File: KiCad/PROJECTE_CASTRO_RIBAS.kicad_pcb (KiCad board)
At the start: 2 copper layers, 114.1 x 85.8 mm, 72 parts, among them J1 DE9_Pins, J2 DE9_Pins, J3 Conn_01x05, J4 Conn_01x02_Pin, J5 Conn_01x04_Pin, K1 Fujitsu_FTR-LYAA005x, K2 Fujitsu_FTR-LYAA005x, SW3 SW_Push_Dual, SW4 SW_Push, SW5 SW_Push, U1 LM2596S-12, U2 LM1117DT-3.3, U20 PIC24HJ128GP502, U23 FXTH87, U3 SN65HVD230, U4 MAX3232, U6 FDC2214, Y1 Crystal

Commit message: Pin del micro pel modul RF triat
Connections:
- U20 pad 11: unconnected-(U20-RB4-Pad11) -> RF_data
- U20 pad 21: CNTRL -> unconnected-(U20-RB10-Pad21)
- U20 pad 22: PWM -> unconnected-(U20-RB11-Pad22)
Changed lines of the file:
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@@
 	(net 75 "unconnected-(U20-RA0-Pad2)")
 	(net 76 "unconnected-(U20-RB7-Pad16)")
-	(net 77 "unconnected-(U20-RB4-Pad11)")
+	(net 77 "unconnected-(U20-RB11-Pad22)")
 	(net 78 "unconnected-(U23-N{slash}C-Pad21)")
 	(net 79 "unconnected-(U23-N{slash}C-Pad19)")
@@
 	(net 90 "unconnected-(U23-PTA3-Pad18)")
 	(net 91 "unconnected-(U23-RF-Pad11)")
+	(net 92 "unconnected-(U20-RB10-Pad21)")
+	(net 93 "RF_data")
 	(footprint "Resistor_SMD:R_0805_2012Metric"
 		(layer "F.Cu")
@@
 			(layers "F.Cu" "F.Mask" "F.Paste")
 			(roundrect_rratio 0.25)
-			(net 77 "unconnected-(U20-RB4-Pad11)")
+			(net 93 "RF_data")
 			(pinfunction "RB4")
-			(pintype "bidirectional+no_connect")
+			(pintype "bidirectional")
 		)
 		(pad "12" smd roundrect
@@
 			(layers "F.Cu" "F.Mask" "F.Paste")
 			(roundrect_rratio 0.25)
-			(net 56 "CNTRL")
+			(net 92 "unconnected-(U20-RB10-Pad21)")
 			(pinfunction "RB10")
-			(pintype "bidirectional")
+			(pintype "bidirectional+no_connect")
 		)
 		(pad "22" smd roundrect
@@
 			(layers "F.Cu" "F.Mask" "F.Paste")
 			(roundrect_rratio 0.25)
-			(net 55 "PWM")
+			(net 77 "unconnected-(U20-RB11-Pad22)")
 			(pinfunction "RB11")
-			(pintype "bidirectional")
+			(pintype "bidirectional+no_connect")
 		)
 		(pad "23" smd roundrect

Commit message: Posicionament fet
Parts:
- moved TP8 134.2 mm to (194.0, 103.5)
- moved C32 132.9 mm to (209.2, 114.0), turned to 90 degrees
- moved L1 131.1 mm to (201.5, 120.2), turned to -90 degrees
- moved TP9 130.1 mm to (192.2, 73.8), turned to 180 degrees
- moved C33 127.1 mm to (204.3, 108.8)
- moved C20 122.6 mm to (197.2, 120.0), turned to -90 degrees
- moved R5 118.3 mm to (193.2, 127.5), turned to 180 degrees
- moved TP1 114.1 mm to (169.0, 58.0)
- moved R9 114.1 mm to (180.0, 86.3), turned to -90 degrees
- moved R8 113.4 mm to (174.2, 57.6), turned to -90 degrees
- moved R6 108.1 mm to (168.8, 119.5)
- moved TP7 106.6 mm to (160.8, 65.0)
- moved TP6 105.8 mm to (160.8, 76.8)
- moved R4 99.7 mm to (159.8, 82.8)
- moved TP2 96.8 mm to (151.5, 60.2), turned to 90 degrees
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
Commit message: Capes d'alimentació i GND
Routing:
- added copper zone on F.Cu, net +12V
- added copper zone on F.Cu, net +3.3V
- added copper zone on B.Cu, net GND
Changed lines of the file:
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@@
 		(layer "Edge.Cuts")
+	)
+	(zone
+		(net 2)
+		(net_name "+3.3V")
+		(layer "F.Cu")
+		(hatch edge 0.5)
+		(priority 2)
+		(connect_pads
+			(clearance 0.5)
+		)
+		(min_thickness 0.25)
+		(filled_areas_thickness no)
+		(fill yes
+			(thermal_gap 0.5)
+			(thermal_bridge_width 0.5)
+		)
+		(polygon
+			(pts
+				(xy 149 80.5) (xy 115.25 80.5) (xy 115.25 72.75) (xy 104.25 72.75) (xy 104.25 61.5) (xy 100.25 61.5)
+				(xy 100.25 128.75) (xy 211 128.75) (xy 211 107.5) (xy 183.75 107.5) (xy 183.75 84.25) (xy 177.25 84.25)
+				(xy 177.25 72.25) (xy 184 72.25) (xy 184 55.25) (xy 167.5 55.25) (xy 167.5 64.25) (xy 149 64.25)
+			)
+		)
+	)
+	(zone
+		(net 17)
+		(net_name "+12V")
+		(layer "F.Cu")
+		(hatch edge 0.5)
+		(priority 1)
+		(connect_pads
+			(clearance 0.5)
+		)
+		(min_thickness 0.25)
+		(filled_areas_thickness no)
+		(fill yes
+			(thermal_gap 0.5)
+			(thermal_bridge_width 0.5)
+		)
+		(polygon
+			(pts
+				(xy 184.5 106.5) (xy 184.5 83) (xy 178.5 83) (xy 178.5 73.75) (xy 184.5 73.75) (xy 184.5 54.5) (xy 167 54.5)
+				(xy 167 63.5) (xy 148 63.5) (xy 148 79.5) (xy 117 79.5) (xy 117 71.5) (xy 105.5 71.5) (xy 105.5 60)
+				(xy 100.25 60) (xy 100.25 45.25) (xy 211.25 45.25) (xy 211.25 106.5)
+			)
+		)
+	)
+	(zone
+		(net 1)
+		(net_name "GND")
+		(layer "B.Cu")
+		(hatch edge 0.5)
+		(connect_pads
+			(clearance 0.5)
+		)
+		(min_thickness 0.25)
+		(filled_areas_thickness no)
+		(fill yes
+			(thermal_gap 0.5)
+			(thermal_bridge_width 0.5)
+		)
+		(polygon
+			(pts
+				(xy 99.25 44.75) (xy 211.75 44.75) (xy 211.75 129.5) (xy 99 129.5)
+			)
+		)
 	)
 	(embedded_fonts no)

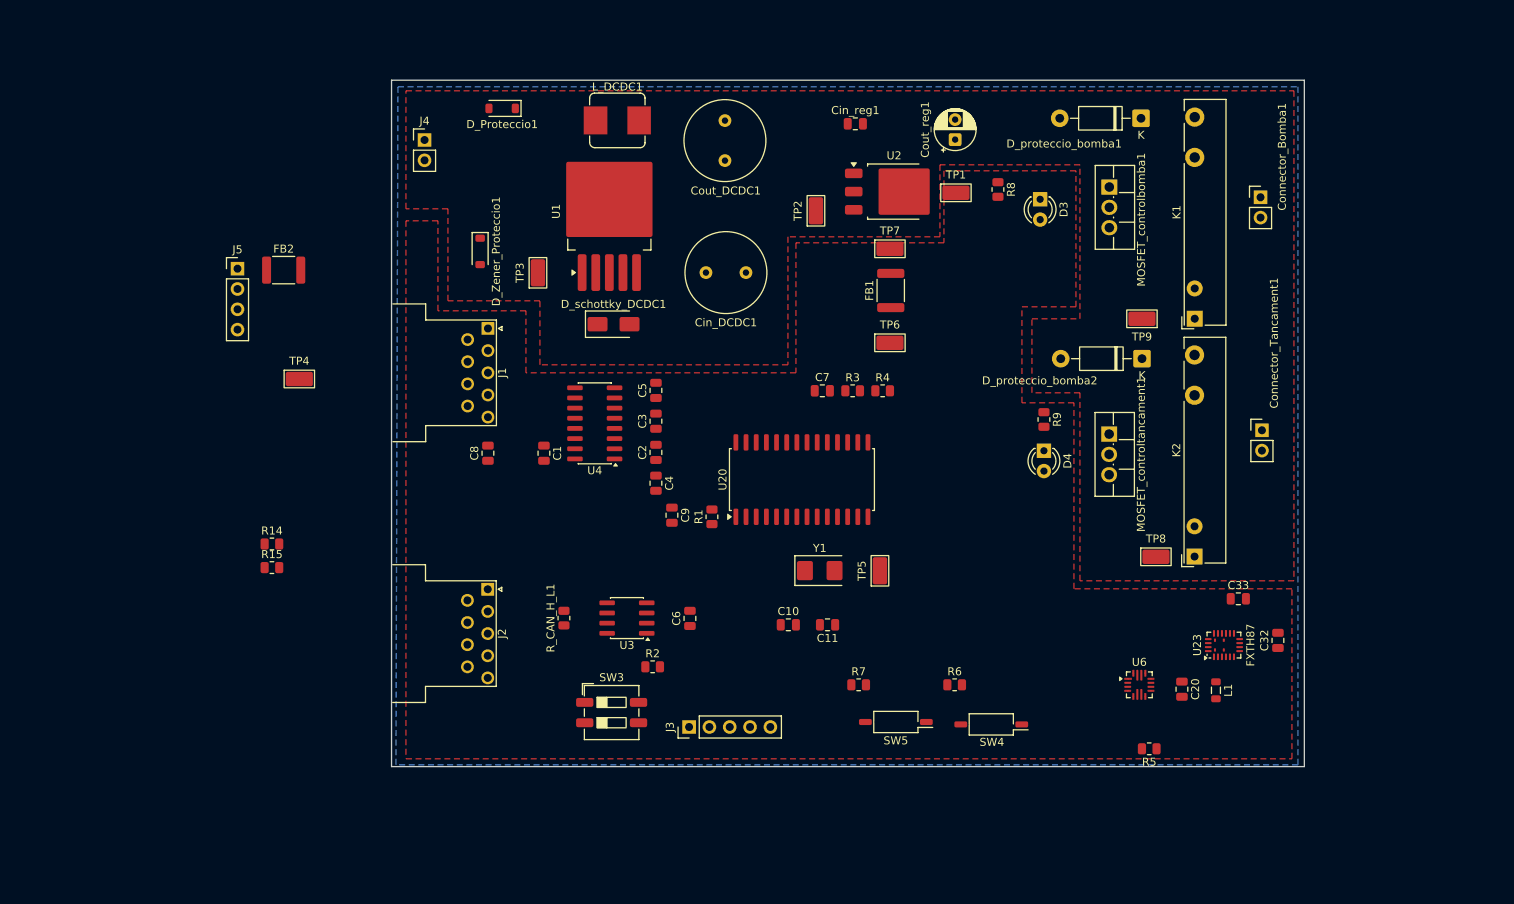
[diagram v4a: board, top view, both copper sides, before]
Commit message: Routing de l'alimentació fet, s'ha afegit connector del mòdul RF i plànols millorats
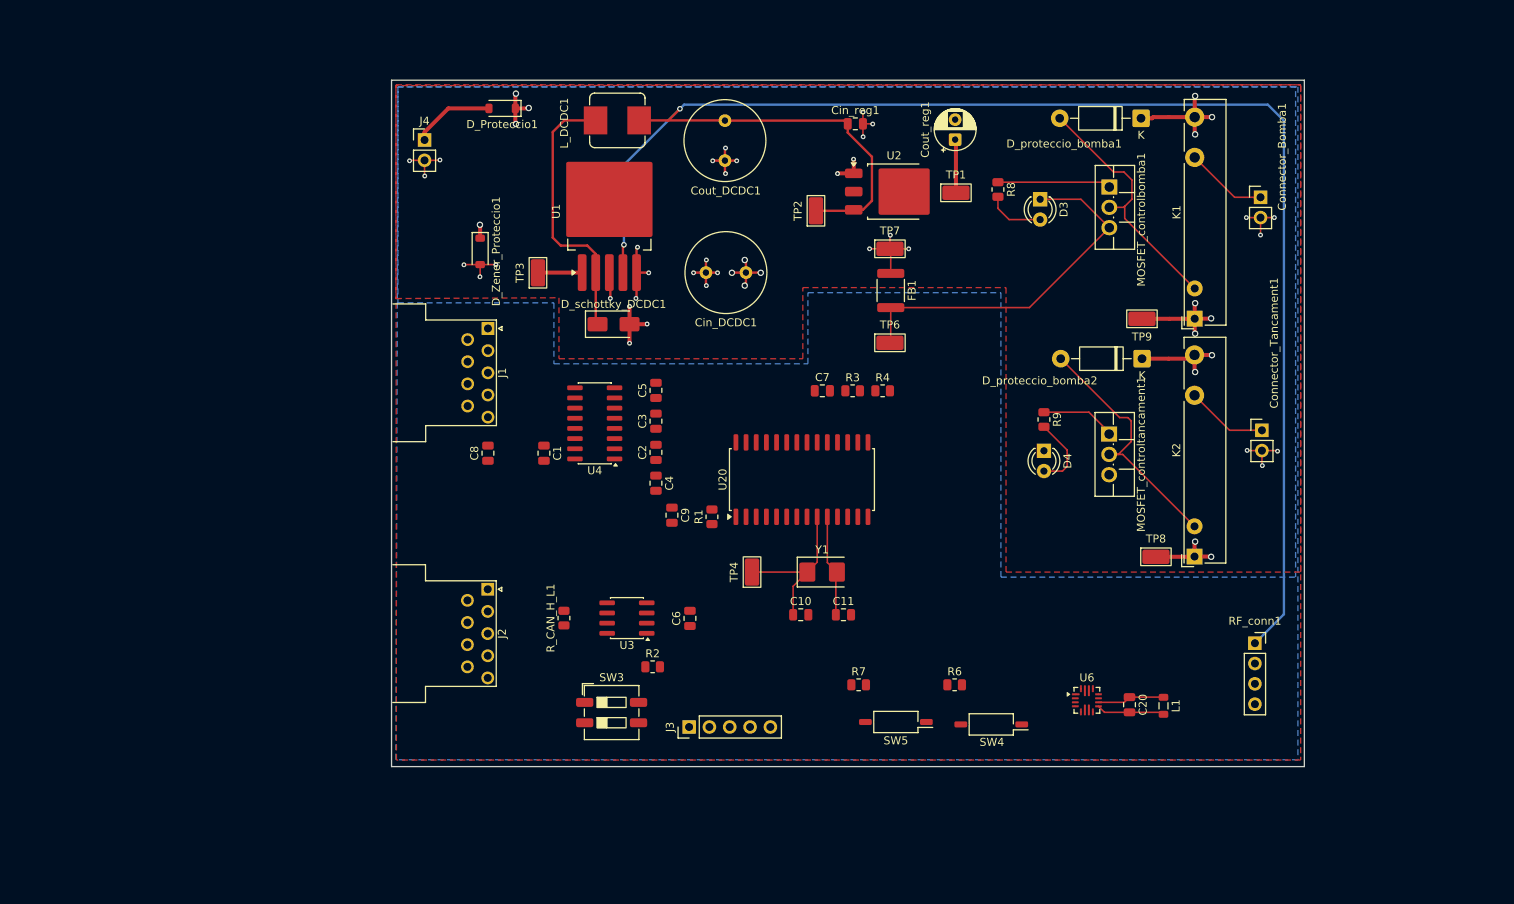
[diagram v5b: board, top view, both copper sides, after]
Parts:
- removed C32, C33: 100nF, Capacitor_SMD:C_0805_2012Metric
- removed FB2: FerriteBead, Inductor_SMD:L_1812_4532Metric
- removed J5: Conn_01x04_Pin, Connector_PinHeader_2.54mm:PinHeader_1x04_P2.54mm_Vertical
- removed R14, R15, R5: 10k, Resistor_SMD:R_0805_2012Metric
- removed TP5: Tp_Osc_OUT, TestPoint:TestPoint_Keystone_5015_Micro_Mini
- removed U23: FXTH87, Package_DFN_QFN:UDC-QFN-20-4EP_3x4mm_P0.5mm_EP0.41x0.25mm
- added RF_conn1: Conn_01x04_Pin, Connector_PinSocket_2.54mm:PinSocket_1x04_P2.54mm_Vertical, F.Cu at (206.4, 114.3)
- moved TP4 61.5 mm to (143.5, 105.4), turned to 90 degrees
- moved C20 6.84 mm to (190.7, 122.0)
- moved L1 6.84 mm to (194.9, 122.1)
- moved U6 6.84 mm to (185.4, 121.4)
- moved C11 2.35 mm to (154.9, 110.7), turned to 0 degrees
- moved C10 1.99 mm to (149.6, 110.7)
- moved Y1 0.35 mm to (152.3, 105.4)
- turned FB1 to -90 degrees
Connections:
- net Net-(U1-FB) renamed +5V
- Cin_DCDC1 pad 2: GND -> GNDPWR
- Cin_reg1 pad 2: GND -> GNDPWR
- Cout_DCDC1 pad 2: GND -> GNDPWR
- D_Zener_Proteccio1 pad 2: GND -> GNDPWR
- D_schottky_DCDC1 pad 2: GND -> GNDPWR
- FB1 pad 1: GND -> GNDPWR
- FB1 pad 2: GNDPWR -> GND
- J4 pad 2: GND -> GNDPWR
- U1 pad 3: GND -> GNDPWR
- U1 pad 5: GND -> GNDPWR
- U2 pad 1: GND -> GNDPWR
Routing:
- net +5V: track 0.00 -> 213.5 mm, vias 0 -> 2
- net GNDPWR: track 0.00 -> 71.4 mm, vias 0 -> 35
- net +12V: track 0.00 -> 66.0 mm, vias 0 -> 18
- net GND: track 0.00 -> 46.0 mm
- net Net-(D_schottky_DCDC1-K): track 0.00 -> 34.2 mm
- net Net-(D_proteccio_bomba2-A): track 0.00 -> 32.4 mm
- net Net-(D_proteccio_bomba1-A): track 0.00 -> 31.7 mm
- net OSC_IN: track 0.00 -> 20.4 mm
- net DO_control_bomba: track 0.00 -> 14.2 mm
- net OSC_OUT: track 0.00 -> 12.8 mm
- net Net-(Connector_Bomba1-Pin_1): track 0.00 -> 10.3 mm
- net Net-(D_Proteccio1-A): track 0.00 -> 10.3 mm
- net Net-(Connector_Tancament1-Pin_1): track 0.00 -> 10.2 mm
- net DO_control_tancament: track 0.00 -> 9.41 mm
- net Net-(D4-A): track 0.00 -> 9.29 mm
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- added copper zone on B.Cu, net GNDPWR

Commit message: Ruteig V1 fet però falta repassar
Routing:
- net GND: track 46.0 -> 150.1 mm, vias 0 -> 43
- net RF_data: track 0.00 -> 64.0 mm, vias 0 -> 2
- net DO_control_bomba: track 14.2 -> 70.8 mm, vias 0 -> 2
- net SCL: track 0.00 -> 51.9 mm
- net SDA: track 0.00 -> 51.4 mm
- net PULS_START: track 0.00 -> 49.1 mm
- net +3.3V: track 6.69 -> 53.3 mm, vias 0 -> 1
- net PGC: track 0.00 -> 43.0 mm, vias 0 -> 2
- net PULS_STOP: track 0.00 -> 43.0 mm, vias 0 -> 2
- net C1TX: track 0.00 -> 42.3 mm
- net C1RX: track 0.00 -> 40.6 mm
- net PGD: track 0.00 -> 40.4 mm
- net MCLR: track 0.00 -> 39.7 mm
- net DO_control_tancament: track 9.41 -> 48.9 mm, vias 0 -> 2
- net TX: track 0.00 -> 34.8 mm, vias 0 -> 2
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
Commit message: TOT enrutat, falta donar una ullada
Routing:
- net +3.3V: track 53.3 -> 107.0 mm, vias 1 -> 9
- net GNDPWR: track 72.2 -> 76.1 mm, vias 35 -> 39
- net GND: track 150.1 -> 151.9 mm, vias 43 -> 44

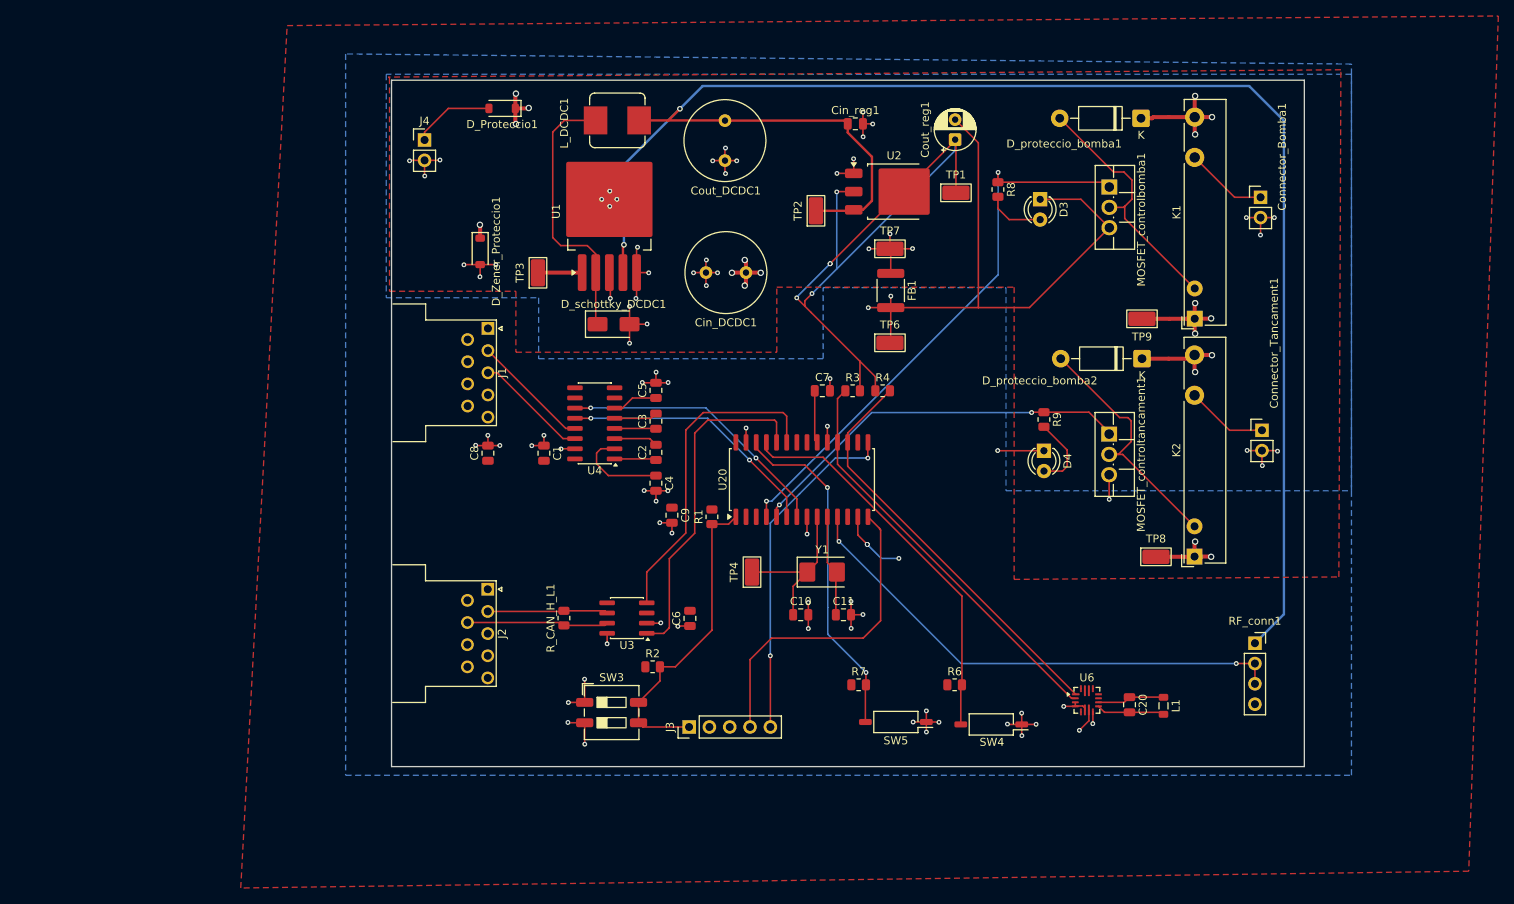
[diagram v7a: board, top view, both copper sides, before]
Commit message: Petits canvis a les regles de disseny i ja no hi ha cap error (hi han avisos)
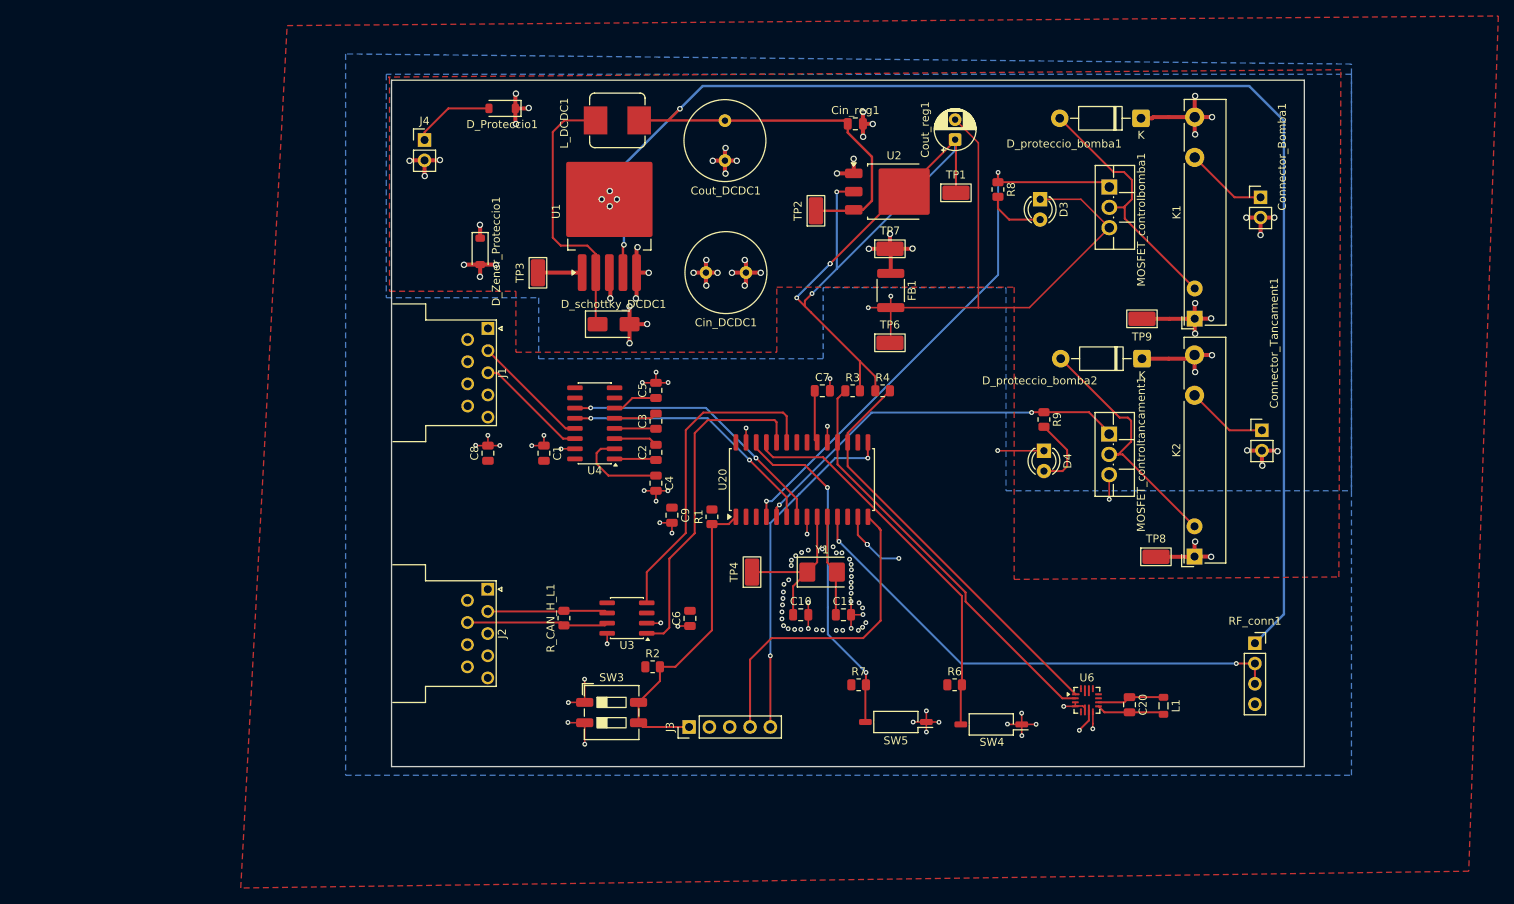
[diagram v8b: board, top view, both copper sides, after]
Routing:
- net SDA: track 51.4 -> 52.1 mm
- net GND: track 151.9 -> 152.5 mm, vias 44 -> 45
- net (no net): vias 0 -> 35
